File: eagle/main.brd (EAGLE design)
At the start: 72.4 x 41.3 mm, 16 parts, among them IC1 74HC164D, IC2 74LS139D, Q1 BSS84, Q2 BSS84, Q3 BSS84

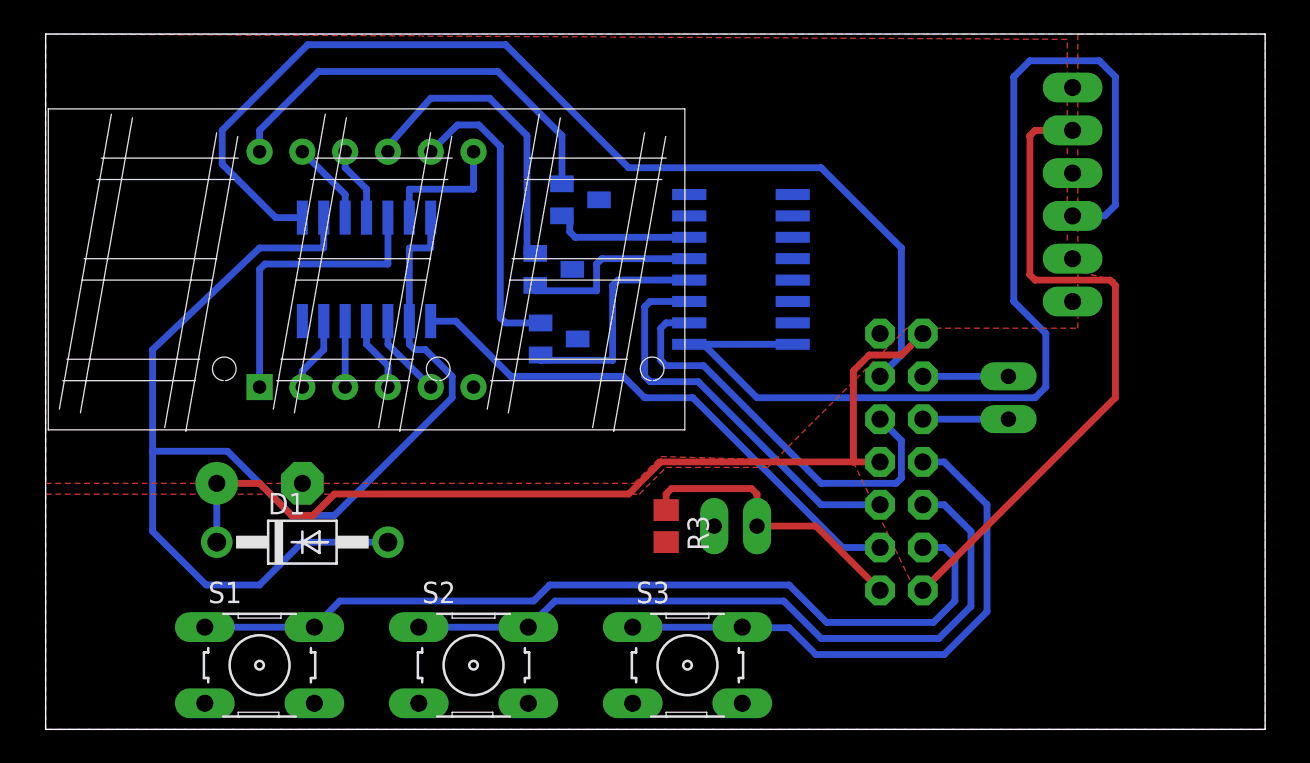
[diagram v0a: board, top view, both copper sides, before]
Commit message: The 430 might not blow up after these edits
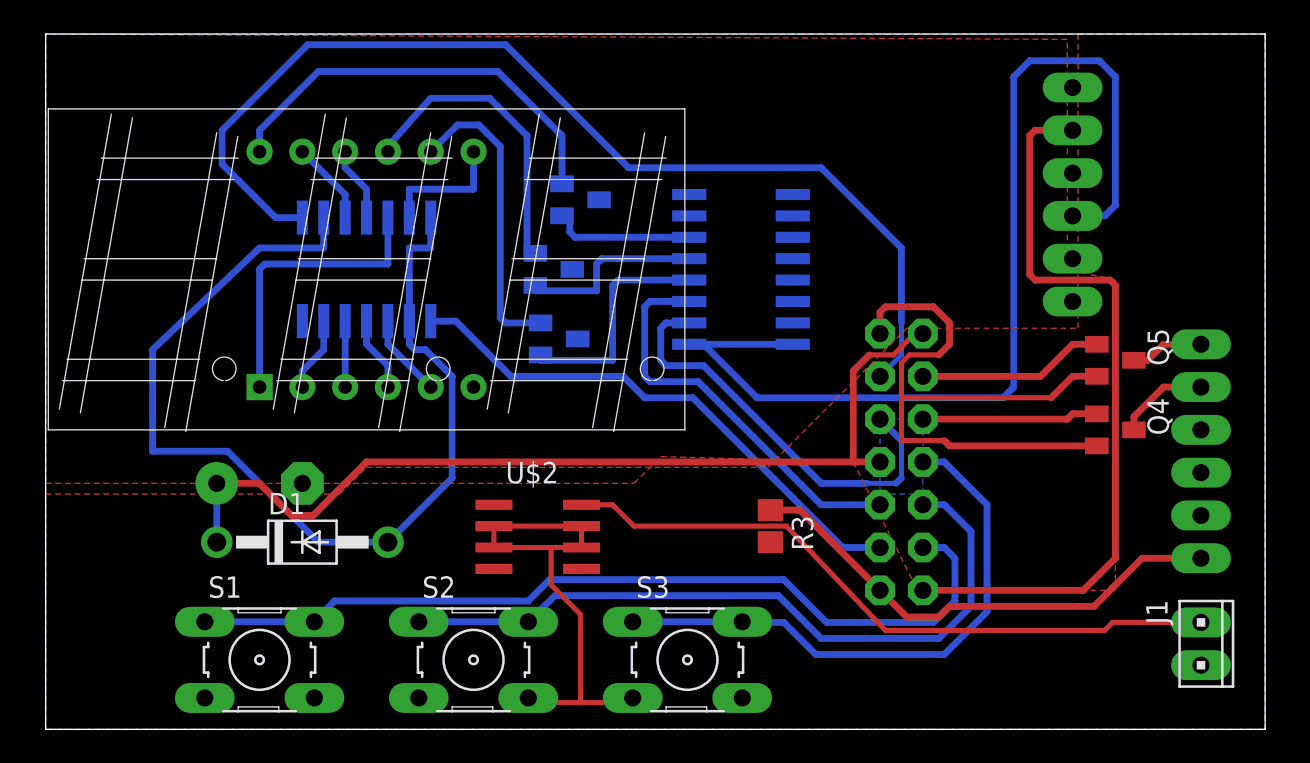
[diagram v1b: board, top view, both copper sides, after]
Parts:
- removed SL1, SL2: (no value), con-amp-quick:02P
- added J1: (no value), con-amp:10X02MTA
- added JP2: (no value), pinhead:1X06
- added Q4, Q5: BSS123, transistor-small-signal:SOT23
- added U$2: L78L33ABD, mjg:SO8
- moved R3 6.19 mm to (43.0, 12.1)
- moved S1 0.32 mm to (12.7, 4.13)
- moved S2 0.32 mm to (25.4, 4.13)
- moved S3 0.32 mm to (38.1, 4.13)
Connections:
- new net N$23: JP2.5, Q4.3
- new net N$28: JP2.6, Q5.3
- new net N$30: J1.2, U$2.8
- net GND: now also J1.1, JP2.2, JP2.3, Q4.2, Q5.2, U$2.2, U$2.3, U$2.6, U$2.7; no longer SL1.1
- net N$17: now also JP2.1; no longer SL1.2
- net N$19: now also Q5.1; no longer SL2.2
- net N$20: now also Q4.1; no longer SL2.1
- net VCC: now also U$2.1
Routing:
- net GND: track 0.00 -> 67.7 mm
- net N$30: track 0.00 -> 40.2 mm
- net VCC: track 141.6 -> 121.9 mm
- net N$17: track 17.4 -> 29.6 mm
- net N$19: track 5.08 -> 11.1 mm
- net N$24: track 39.1 -> 44.7 mm
- net N$23: track 0.00 -> 5.49 mm
- net N$20: track 5.08 -> 10.5 mm
- net N$28: track 0.00 -> 4.37 mm
- net N$18: track 34.0 -> 34.7 mm
- added copper zone on layer 16, net N$22

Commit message: updated values and added example parts order for Newark
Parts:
- C1: value (none) -> 1F
- R3: value (none) -> 720ish
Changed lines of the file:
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@@
 <element name="U$1" library="mjg" package="BL-T52X-31" value="BL-T52C-31" x="19.05" y="27.305"/>
 <element name="IC1" library="74xx-us" package="SO14" value="74HC164D" x="19.05" y="27.305" rot="MR0"/>
-<element name="C1" library="rcl" package="E5-13" value="" x="12.7" y="14.605" rot="MR180"/>
+<element name="C1" library="rcl" package="E5-13" value="1F" x="12.7" y="14.605" rot="MR180"/>
 <element name="D1" library="diode" package="DO41-10" value="1N4004" x="15.24" y="11.1125"/>
-<element name="R3" library="rcl" package="R0805" value="" x="43.02125" y="12.065" rot="R270"/>
+<element name="R3" library="rcl" package="R0805" value="720ish" x="43.02125" y="12.065" rot="R270"/>
 <element name="JP1" library="pinhead" package="1X06/90" value="" x="64.77" y="31.75" rot="MR90"/>
 <element name="S1" library="switch-omron" package="B3F-10XX" value="" x="12.7" y="4.1275">

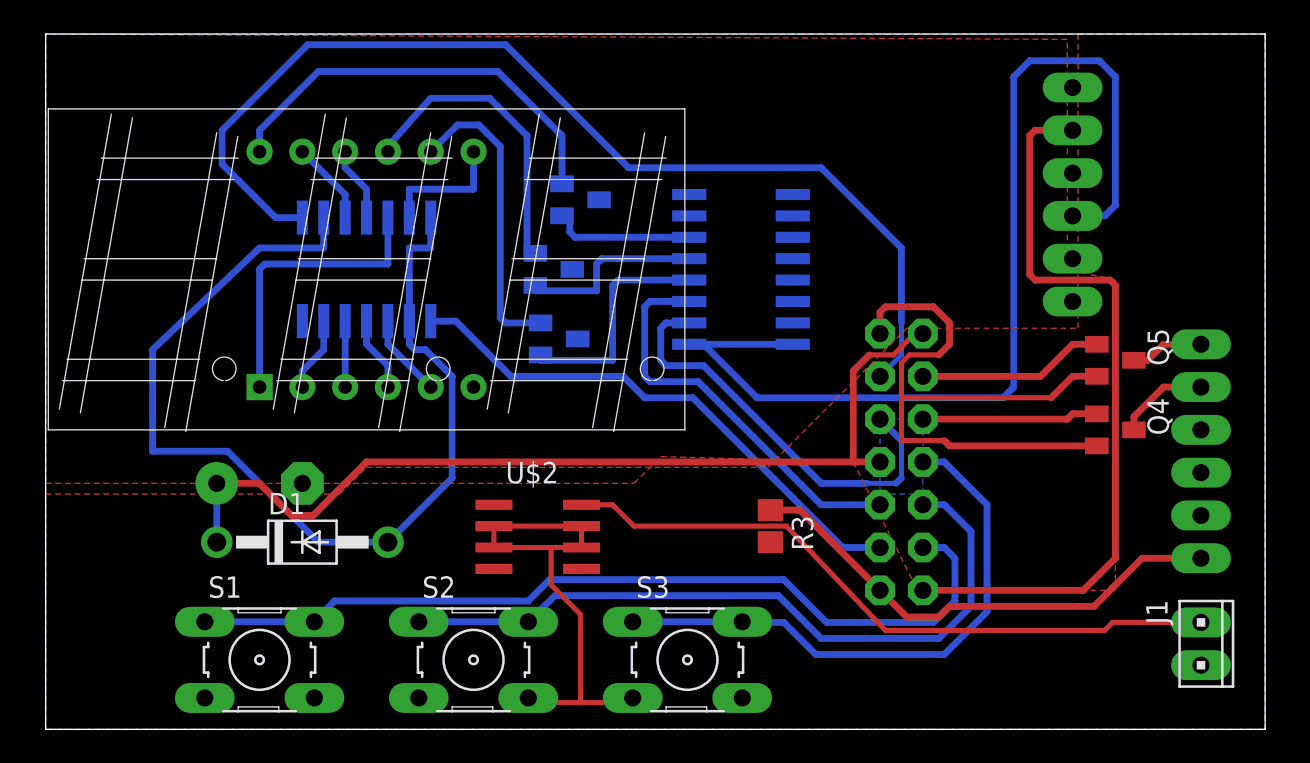
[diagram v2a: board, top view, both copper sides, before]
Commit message: added hole pattern. ready to print, i think.
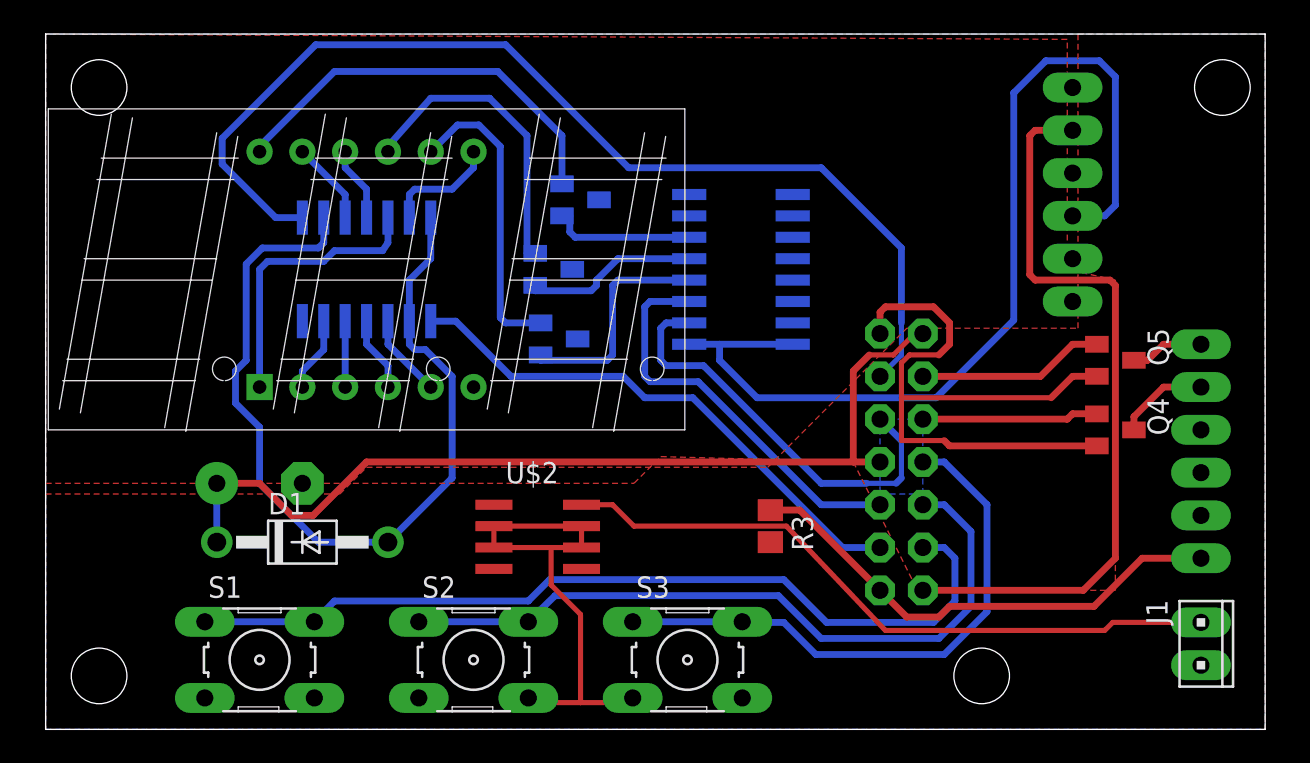
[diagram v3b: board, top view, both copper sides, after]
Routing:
- net VCC: track 121.9 -> 110.9 mm
- net N$8: track 7.72 -> 6.79 mm
- net N$26: track 11.2 -> 10.4 mm
- net N$4: track 17.5 -> 16.8 mm
- net N$11: track 25.1 -> 24.5 mm
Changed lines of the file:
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@@
 <layer number="43" name="vRestrict" color="2" fill="10" visible="no" active="yes"/>
 <layer number="44" name="Drills" color="7" fill="1" visible="no" active="yes"/>
-<layer number="45" name="Holes" color="7" fill="1" visible="no" active="yes"/>
+<layer number="45" name="Holes" color="7" fill="1" visible="yes" active="yes"/>
 <layer number="46" name="Milling" color="3" fill="1" visible="no" active="yes"/>
 <layer number="47" name="Measures" color="7" fill="1" visible="no" active="yes"/>
@@
 <wire x1="72.39" y1="41.275" x2="72.39" y2="0" width="0.040640625" layer="20"/>
 <wire x1="72.39" y1="0" x2="0" y2="0" width="0.040640625" layer="20"/>
+<hole x="3.175" y="3.175" drill="3.302"/>
+<hole x="3.175" y="38.1" drill="3.302"/>
+<hole x="69.85" y="38.1" drill="3.302"/>
+<hole x="55.5625" y="3.175" drill="3.302"/>
 </plain>
 <attributes>
@@
 <contactref element="IC1" pad="13"/>
 <contactref element="U$1" pad="P$12"/>
-<wire x1="21.59" y1="30.3784" x2="21.59" y2="32.0675" width="0.4064" layer="16"/>
-<wire x1="21.59" y1="32.0675" x2="25.4" y2="32.0675" width="0.4064" layer="16"/>
-<wire x1="25.4" y1="32.0675" x2="25.4" y2="34.29" width="0.4064" layer="16"/>
+<wire x1="21.59" y1="30.3784" x2="21.59" y2="31.75" width="0.4064" layer="16"/>
+<wire x1="21.59" y1="31.75" x2="21.9075" y2="32.0675" width="0.4064" layer="16"/>
+<wire x1="21.9075" y1="32.0675" x2="24.13" y2="32.0675" width="0.4064" layer="16"/>
+<wire x1="24.13" y1="32.0675" x2="25.4" y2="33.3375" width="0.4064" layer="16"/>
+<wire x1="25.4" y1="33.3375" x2="25.4" y2="34.29" width="0.4064" layer="16"/>
 </signal>
 <signal name="N$9">
@@
 <contactref element="U$1" pad="P$7"/>
 <contactref element="Q1" pad="2"/>
-<wire x1="12.7" y1="34.29" x2="12.7" y2="35.56" width="0.4064" layer="16"/>
-<wire x1="12.7" y1="35.56" x2="16.1925" y2="39.0525" width="0.4064" layer="16"/>
-<wire x1="16.1925" y1="39.0525" x2="26.84" y2="39.0525" width="0.4064" layer="16"/>
+<wire x1="12.7" y1="34.29" x2="12.7" y2="34.6075" width="0.4064" layer="16"/>
+<wire x1="12.7" y1="34.6075" x2="17.145" y2="39.0525" width="0.4064" layer="16"/>
+<wire x1="17.145" y1="39.0525" x2="26.84" y2="39.0525" width="0.4064" layer="16"/>
 <wire x1="26.84" y1="39.0525" x2="30.65" y2="35.2425" width="0.4064" layer="16"/>
 <wire x1="30.65" y1="35.2425" x2="30.65" y2="32.3825" width="0.4064" layer="16"/>
@@
 <wire x1="15.24" y1="30.3784" x2="13.6525" y2="30.3784" width="0.4064" layer="16"/>
 <wire x1="13.6525" y1="30.3784" x2="10.4775" y2="33.5534" width="0.4064" layer="16"/>
-<wire x1="10.4775" y1="33.5534" x2="10.4775" y2="35.56" width="0.4064" layer="16"/>
-<wire x1="10.4775" y1="35.56" x2="15.5575" y2="40.64" width="0.4064" layer="16"/>
-<wire x1="15.5575" y1="40.64" x2="27.305" y2="40.64" width="0.4064" layer="16"/>
+<wire x1="10.4775" y1="33.5534" x2="10.4775" y2="35.08375" width="0.4064" layer="16"/>
+<wire x1="10.4775" y1="35.08375" x2="16.03375" y2="40.64" width="0.4064" layer="16"/>
+<wire x1="16.03375" y1="40.64" x2="27.305" y2="40.64" width="0.4064" layer="16"/>
 <wire x1="27.305" y1="40.64" x2="34.6075" y2="33.3375" width="0.4064" layer="16"/>
 <wire x1="34.6075" y1="33.3375" x2="46.0375" y2="33.3375" width="0.4064" layer="16"/>
@@
 <contactref element="IC1" pad="14"/>
 <contactref element="IC2" pad="16"/>
-<wire x1="21.59" y1="24.2316" x2="21.59" y2="28.575" width="0.4064" layer="16"/>
-<wire x1="21.59" y1="28.575" x2="22.86" y2="28.575" width="0.4064" layer="16"/>
-<wire x1="22.86" y1="28.575" x2="22.86" y2="30.3784" width="0.4064" layer="16"/>
+<wire x1="21.59" y1="24.2316" x2="21.59" y2="26.67" width="0.4064" layer="16"/>
+<wire x1="21.59" y1="26.67" x2="22.86" y2="27.94" width="0.4064" layer="16"/>
+<wire x1="22.86" y1="27.94" x2="22.86" y2="30.3784" width="0.4064" layer="16"/>
 <polygon width="0.3048" layer="1">
 <vertex x="0" y="0"/>
@@
 <wire x1="21.9075" y1="22.5425" x2="22.5425" y2="22.5425" width="0.4064" layer="16"/>
 <wire x1="22.5425" y1="22.5425" x2="24.13" y2="20.955" width="0.4064" layer="16"/>
-<wire x1="44.3484" y1="22.86" x2="39.0525" y2="22.86" width="0.4064" layer="16"/>
-<wire x1="16.51" y1="30.3784" x2="16.51" y2="28.575" width="0.4064" layer="16"/>
-<wire x1="16.51" y1="28.575" x2="12.7" y2="28.575" width="0.4064" layer="16"/>
-<wire x1="12.7" y1="28.575" x2="6.35" y2="22.5425" width="0.4064" layer="16"/>
-<wire x1="6.35" y1="22.5425" x2="6.35" y2="16.51" width="0.4064" layer="16"/>
-<wire x1="6.35" y1="16.51" x2="10.795" y2="16.51" width="0.4064" layer="16"/>
-<wire x1="10.795" y1="16.51" x2="16.1925" y2="11.1125" width="0.4064" layer="16"/>
+<wire x1="44.3484" y1="22.86" x2="40.005" y2="22.86" width="0.4064" layer="16"/>
+<wire x1="16.51" y1="30.3784" x2="16.51" y2="28.8925" width="0.4064" layer="16"/>
+<wire x1="16.51" y1="28.8925" x2="16.1925" y2="28.575" width="0.4064" layer="16"/>
+<wire x1="16.1925" y1="28.575" x2="12.85875" y2="28.575" width="0.4064" layer="16"/>
+<wire x1="12.85875" y1="28.575" x2="11.90625" y2="27.6225" width="0.4064" layer="16"/>
+<wire x1="11.90625" y1="27.6225" x2="11.90625" y2="21.9075" width="0.4064" layer="16"/>
+<wire x1="11.90625" y1="21.9075" x2="11.27125" y2="21.2725" width="0.4064" layer="16"/>
+<wire x1="11.27125" y1="21.2725" x2="11.27125" y2="19.3675" width="0.4064" layer="16"/>
+<wire x1="11.27125" y1="19.3675" x2="12.7" y2="17.93875" width="0.4064" layer="16"/>
+<wire x1="12.7" y1="17.93875" x2="12.7" y2="14.605" width="0.4064" layer="16"/>
+<wire x1="12.7" y1="14.605" x2="16.1925" y2="11.1125" width="0.4064" layer="16"/>
 <wire x1="16.1925" y1="11.1125" x2="20.32" y2="11.1125" width="0.4064" layer="16"/>
-<wire x1="38.2016" y1="22.86" x2="39.0525" y2="22.86" width="0.4064" layer="16"/>
-<wire x1="39.0525" y1="22.86" x2="42.2275" y2="19.685" width="0.4064" layer="16"/>
-<wire x1="42.2275" y1="19.685" x2="56.8325" y2="19.685" width="0.4064" layer="16"/>
-<wire x1="56.8325" y1="19.685" x2="57.4675" y2="20.32" width="0.4064" layer="16"/>
-<wire x1="57.4675" y1="20.32" x2="57.4675" y2="38.735" width="0.4064" layer="16"/>
-<wire x1="57.4675" y1="38.735" x2="58.42" y2="39.6875" width="0.4064" layer="16"/>
-<wire x1="58.42" y1="39.6875" x2="62.5475" y2="39.6875" width="0.4064" layer="16"/>
+<wire x1="38.2016" y1="22.86" x2="40.005" y2="22.86" width="0.4064" layer="16"/>
+<wire x1="40.005" y1="22.86" x2="40.005" y2="21.9075" width="0.4064" layer="16"/>
+<wire x1="40.005" y1="21.9075" x2="42.2275" y2="19.685" width="0.4064" layer="16"/>
+<wire x1="42.2275" y1="19.685" x2="52.86375" y2="19.685" width="0.4064" layer="16"/>
+<wire x1="52.86375" y1="19.685" x2="57.4675" y2="24.28875" width="0.4064" layer="16"/>
+<wire x1="57.4675" y1="24.28875" x2="57.4675" y2="37.7825" width="0.4064" layer="16"/>
+<wire x1="57.4675" y1="37.7825" x2="59.3725" y2="39.6875" width="0.4064" layer="16"/>
+<wire x1="59.3725" y1="39.6875" x2="62.5475" y2="39.6875" width="0.4064" layer="16"/>
 <wire x1="62.5475" y1="39.6875" x2="63.5" y2="38.735" width="0.4064" layer="16"/>
 <wire x1="63.5" y1="38.735" x2="63.5" y2="31.115" width="0.4064" layer="16"/>
@@
 <contactref element="Q3" pad="1"/>
 <wire x1="29.38" y1="22.2275" x2="29.38" y2="21.9075" width="0.4064" layer="16"/>
-<wire x1="29.38" y1="21.9075" x2="33.655" y2="21.9075" width="0.4064" layer="16"/>
-<wire x1="33.655" y1="21.9075" x2="33.655" y2="26.3525" width="0.4064" layer="16"/>
+<wire x1="29.38" y1="21.9075" x2="33.3375" y2="21.9075" width="0.4064" layer="16"/>
+<wire x1="33.3375" y1="21.9075" x2="33.655" y2="22.225" width="0.4064" layer="16"/>
+<wire x1="33.655" y1="22.225" x2="33.655" y2="26.3525" width="0.4064" layer="16"/>
 <wire x1="33.655" y1="26.3525" x2="33.9725" y2="26.67" width="0.4064" layer="16"/>
 <wire x1="33.9725" y1="26.67" x2="38.2016" y2="26.67" width="0.4064" layer="16"/>
@@
 <contactref element="Q2" pad="1"/>
 <wire x1="29.0625" y1="26.355" x2="29.0625" y2="26.035" width="0.4064" layer="16"/>
-<wire x1="29.0625" y1="26.035" x2="32.7025" y2="26.035" width="0.4064" layer="16"/>
-<wire x1="32.7025" y1="26.035" x2="32.7025" y2="27.6225" width="0.4064" layer="16"/>
-<wire x1="32.7025" y1="27.6225" x2="33.02" y2="27.94" width="0.4064" layer="16"/>
-<wire x1="33.02" y1="27.94" x2="38.2016" y2="27.94" width="0.4064" layer="16"/>
+<wire x1="29.0625" y1="26.035" x2="32.385" y2="26.035" width="0.4064" layer="16"/>
+<wire x1="32.385" y1="26.035" x2="32.7025" y2="26.3525" width="0.4064" layer="16"/>
+<wire x1="32.7025" y1="26.3525" x2="32.7025" y2="26.67" width="0.4064" layer="16"/>
+<wire x1="32.7025" y1="26.67" x2="33.9725" y2="27.94" width="0.4064" layer="16"/>
+<wire x1="33.9725" y1="27.94" x2="38.2016" y2="27.94" width="0.4064" layer="16"/>
 </signal>
 <signal name="N$27">
@@
 <contactref element="IC1" pad="12"/>
 <wire x1="12.7" y1="20.32" x2="12.7" y2="27.305" width="0.4064" layer="16"/>
-<wire x1="12.7" y1="27.305" x2="13.0175" y2="27.6225" width="0.4064" layer="16"/>
-<wire x1="13.0175" y1="27.6225" x2="20.32" y2="27.6225" width="0.4064" layer="16"/>
-<wire x1="20.32" y1="27.6225" x2="20.32" y2="30.3784" width="0.4064" layer="16"/>
+<wire x1="12.7" y1="27.305" x2="13.17625" y2="27.78125" width="0.4064" layer="16"/>
+<wire x1="13.17625" y1="27.78125" x2="16.51" y2="27.78125" width="0.4064" layer="16"/>
+<wire x1="16.51" y1="27.78125" x2="17.145" y2="28.41625" width="0.4064" layer="16"/>
+<wire x1="17.145" y1="28.41625" x2="20.0025" y2="28.41625" width="0.4064" layer="16"/>
+<wire x1="20.0025" y1="28.41625" x2="20.32" y2="28.8925" width="0.4064" layer="16"/>
+<wire x1="20.32" y1="28.8925" x2="20.32" y2="30.3784" width="0.4064" layer="16"/>
 </signal>
 <signal name="N$3">

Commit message: Lots of hw changes and swapped parts.  Maybe your FTDI chip won't blow up with this one.
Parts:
- removed U$2: L78L33ABD, mjg:SO8
- added IC3: 317EMP, linear:SOT223
- moved J1 65.6 mm to (3.17, 10.2)
- moved R3 3.93 mm to (45.7, 9.21), turned to 90 degrees
- moved D1 2.06 mm to (13.2, 11.1)
- moved 430 1.27 mm to (49.5, 15.9)
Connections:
- net GND: now also IC3.1; no longer U$2.2, U$2.3, U$2.6, U$2.7
- net N$30: now also IC3.3; no longer U$2.8
- net VCC: now also IC3.4; no longer JP1.3, U$2.1
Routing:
- net VCC: track 110.9 -> 148.4 mm
- net N$30: track 40.2 -> 7.16 mm
- net GND: track 67.7 -> 43.3 mm
- net N$17: track 29.6 -> 25.0 mm
- net N$15: track 51.9 -> 50.0 mm
- net N$18: track 34.7 -> 33.2 mm
- net N$16: track 43.2 -> 41.7 mm
- net N$21: track 24.0 -> 22.8 mm
- net N$20: track 10.5 -> 11.7 mm
- net N$19: track 11.1 -> 12.4 mm
- net N$12: track 32.2 -> 31.0 mm
- net N$22: track 25.2 -> 23.9 mm
- net N$24: track 44.7 -> 45.3 mm
- net N$13: track 63.4 -> 62.8 mm
- added copper zone on layer 16, net VCC

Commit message: Little tweaks.  warning: scribus file is not consistent due to crashiness.
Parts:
- added R1: 3ish, rcl:R0805
- moved R3 0.79 mm to (45.7, 8.41)
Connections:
- new net N$29: D1.C, R1.2
- net N$14: now also R1.1; no longer D1.C
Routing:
- net VCC: track 148.4 -> 183.1 mm
- net N$22: track 23.9 -> 16.7 mm
- net N$29: track 0.00 -> 2.69 mm
- net N$14: track 55.8 -> 53.9 mm
- net N$18: track 33.2 -> 32.1 mm
- net N$16: track 41.7 -> 40.6 mm
- net N$15: track 50.0 -> 49.3 mm
- net N$21: track 22.8 -> 22.3 mm
- removed copper zone on layer 16, net N$22
